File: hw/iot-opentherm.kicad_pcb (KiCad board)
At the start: 4 copper layers, 20.3 x 66 mm, 32 parts, among them J1 USB_B_Micro, J2 Conn_01x02, J3 Conn_01x03, J4 Conn_02x06_Odd_Even, J5 Conn_01x02, Q1 BC858, U1 AMS1117-3.3, U2 ESP-12S, U3 PC817, U4 PC817

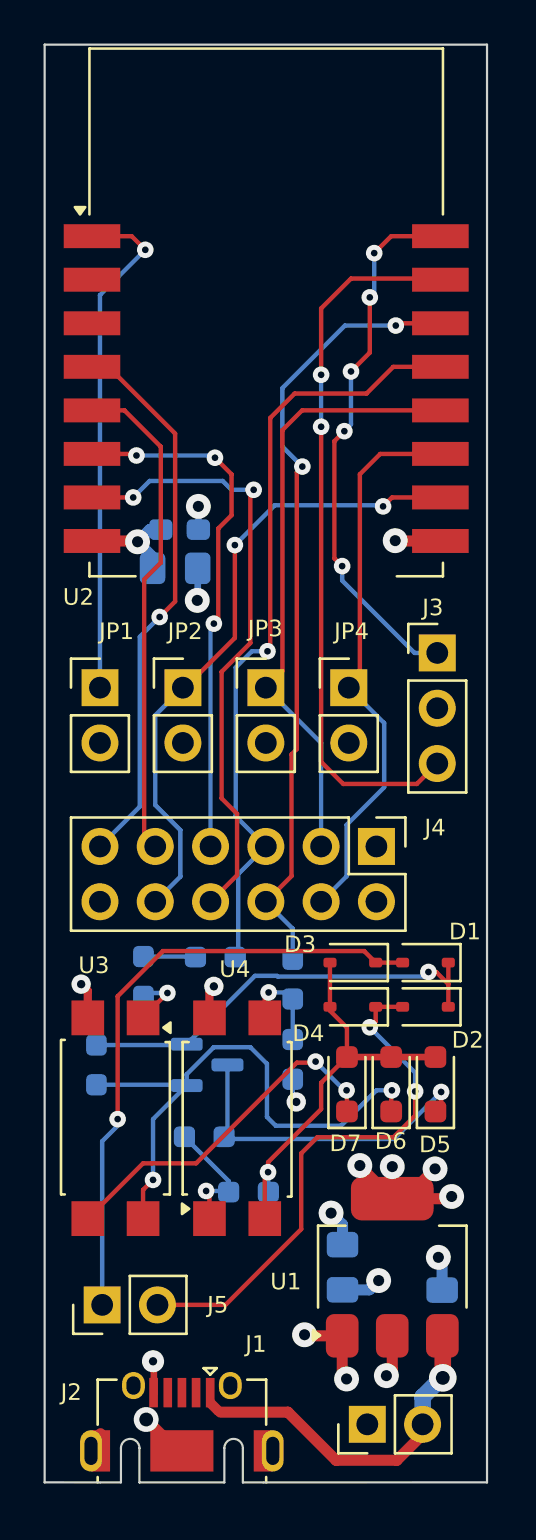
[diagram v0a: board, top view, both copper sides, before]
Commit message: Fixes after running first version
1. Corrected footprint for D1, D2, D3, D4 to bigger one
2. Added connectors for OTx and +5VDC.
3. GPIOs for OT communication swapped to be aligned with Ihor's Melnyk
adapter design and Arthur Rump FW solution
4. Added labels for OTx and +5VDC
5. ERC: no regression
6. DRC: two more issues

Signed-off-by: Zbigniew Lukwinski <elezbyl@gmail.com>
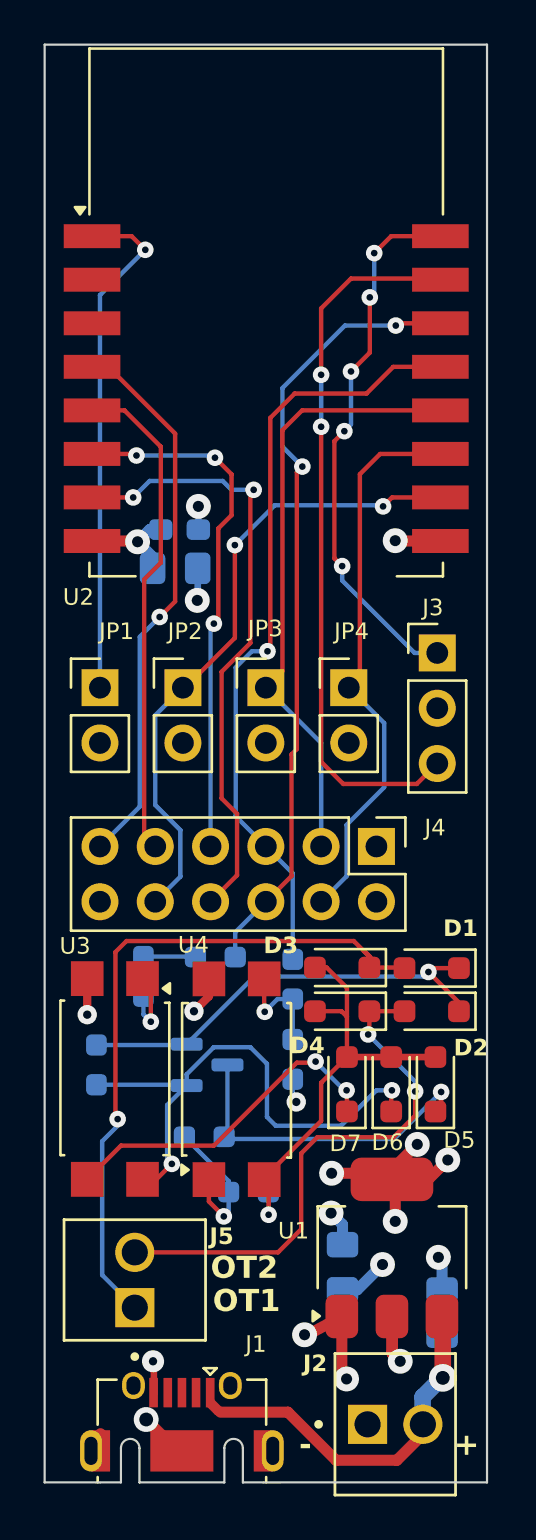
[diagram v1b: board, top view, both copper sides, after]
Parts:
- added REF**: OSHW-Logo2_7.3x6mm_SilkScreen, Symbol:OSHW-Logo2_7.3x6mm_SilkScreen, B.Cu at (130.6, 51.1)
- D1, D2, D3, D4: footprint Diode_SMD:D_SOD-323 -> Diode_SMD:D_SOD-323_HandSoldering
- J2, J5: footprint Connector_PinHeader_2.54mm:PinHeader_1x02_P2.54mm_Vertical -> Connector_TE-Connectivity_:TE_282834-2
- moved J5 1.88 mm to (127.6, 102.8)
- moved U3 1.80 mm to (126.7, 93.6)
- moved U4 1.79 mm to (132.3, 93.6)
- moved J2 1.28 mm to (139.5, 109.5), turned to 0 degrees
- moved U1 0.89 mm to (139.4, 101.4)
- moved D3 0.54 mm to (137.1, 88.5)
- moved D4 0.53 mm to (137.1, 90.5)
- moved D1 0.38 mm to (141.2, 88.5)
- moved D2 0.35 mm to (141.2, 90.5)
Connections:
- R6 pad 1: /GPIO4 -> /GPIO5
- R7 pad 1: /GPIO5 -> /GPIO4
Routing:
- net /OT1: track 28.6 -> 33.2 mm
- net Net-(D3-A): track 18.6 -> 20.6 mm
- net GND: track 20.7 -> 22.3 mm
- net Net-(D6-K): track 26.1 -> 24.9 mm
- net +3.3V: track 19.0 -> 20.1 mm
- net Net-(R2-Pad2): track 5.77 -> 6.56 mm
- net Net-(D7-K): track 16.4 -> 15.7 mm
- net Net-(D1-K): track 19.8 -> 20.5 mm
- net /OUT: track 4.33 -> 4.91 mm
- net Net-(R4-Pad1): track 2.77 -> 3.28 mm
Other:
- board text added: "+"
- board text added: "+5VDC"
- board text added: "-"
- board text added: "IoT OpenTherm, v1.01 Nov, 2024"
- board text added: "OT1"
- board text added: "OT2"
- board text removed: "IoT OpenTherm, v1.00 Oct, 2024"
